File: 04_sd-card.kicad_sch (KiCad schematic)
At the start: 0 parts

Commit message: Adds SD card connector, control buttons and debug headers
Signed-off-by: Anna-Lena Marx <anna-lena.marx@web.de>
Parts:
- added C1: 22u, Capacitor_SMD:C_1206_3216Metric_Pad1.33x1.80mm_HandSolder, symbol Device:C
- added J1: Micro_SD_Card_Det2, Connector_Card:microSD_HC_Hirose_DM3AT-SF-PEJM5, symbol Connector:Micro_SD_Card_Det2
- added R1, R2, R3, R4: 22k, Resistor_SMD:R_1206_3216Metric_Pad1.30x1.75mm_HandSolder, symbol Device:R
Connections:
- new net: C1.2, J1.4 (VDD)
- new net +3.3V: C1.1, R1.1, R2.1, R3.1, R4.1
- new net GND: J1.11 (SHIELD), J1.6 (VSS)
- new net SD_CLK-SCLK: J1.5 (CLK), R2.2
- new net SD_CMD-DI: J1.3 (CMD), R3.2
- new net SD_DAT0-DO: J1.7 (DAT0), R1.2
- new net SD_DAT3-CD-CS: J1.2 (DAT3/CD), R4.2
- no-connect marks 0 -> 4

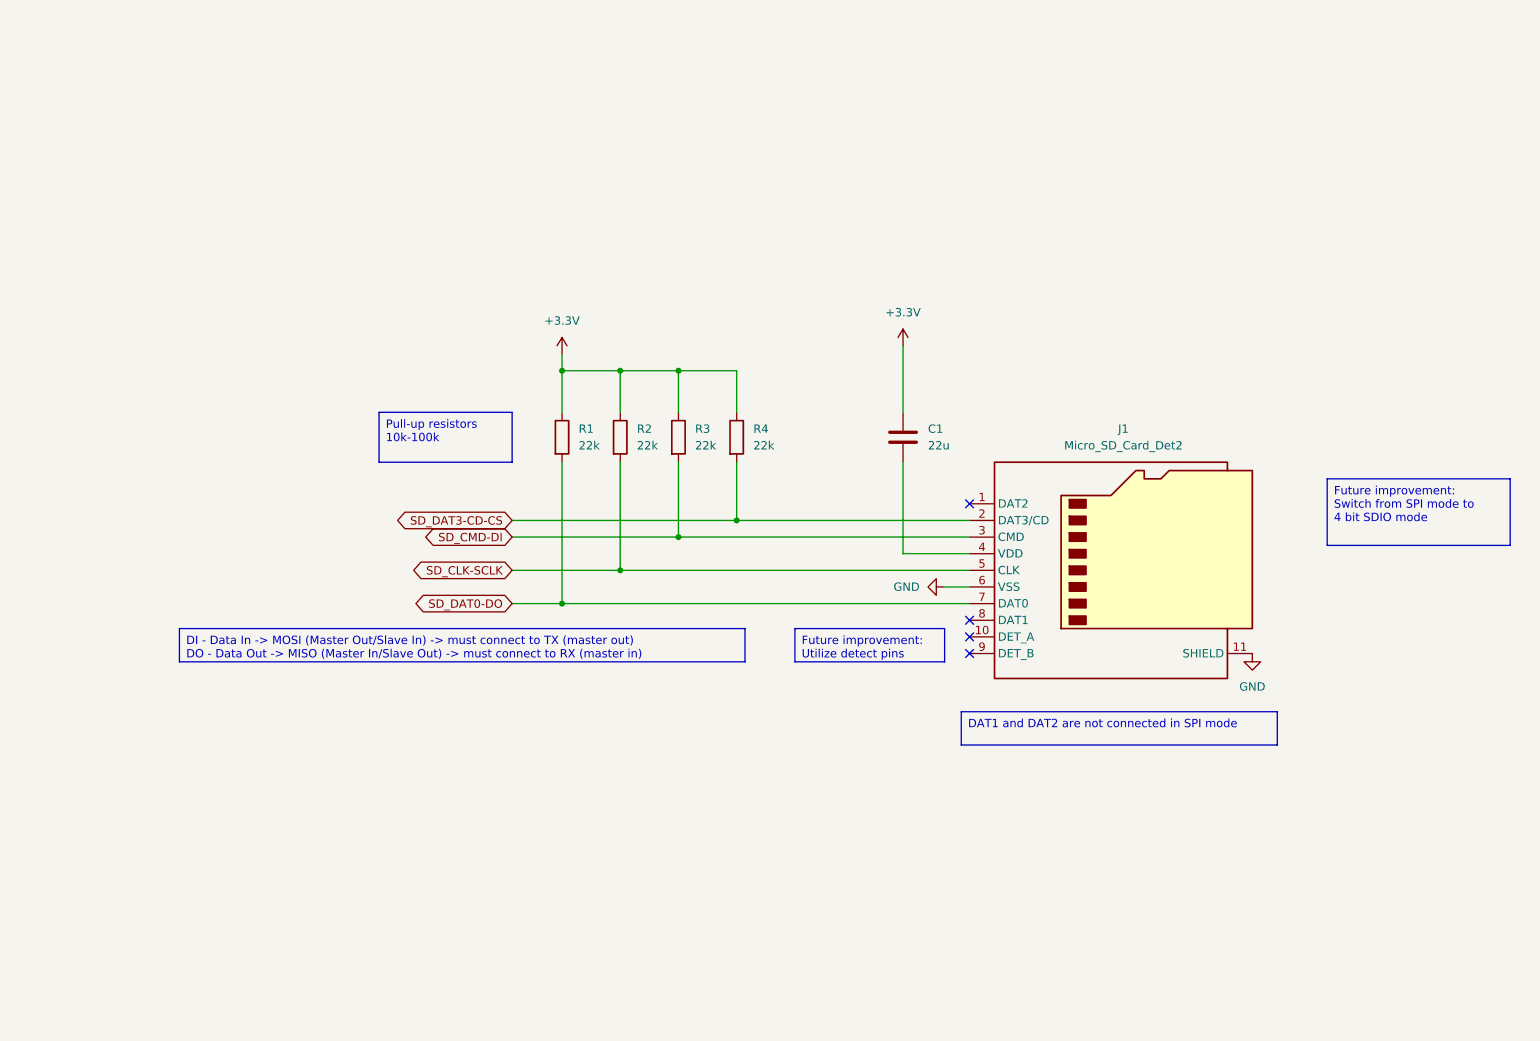
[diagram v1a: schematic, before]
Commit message: Add EPD Driver Circuit
Signed-off-by: Anna-Lena Marx <anna-lena.marx@web.de>
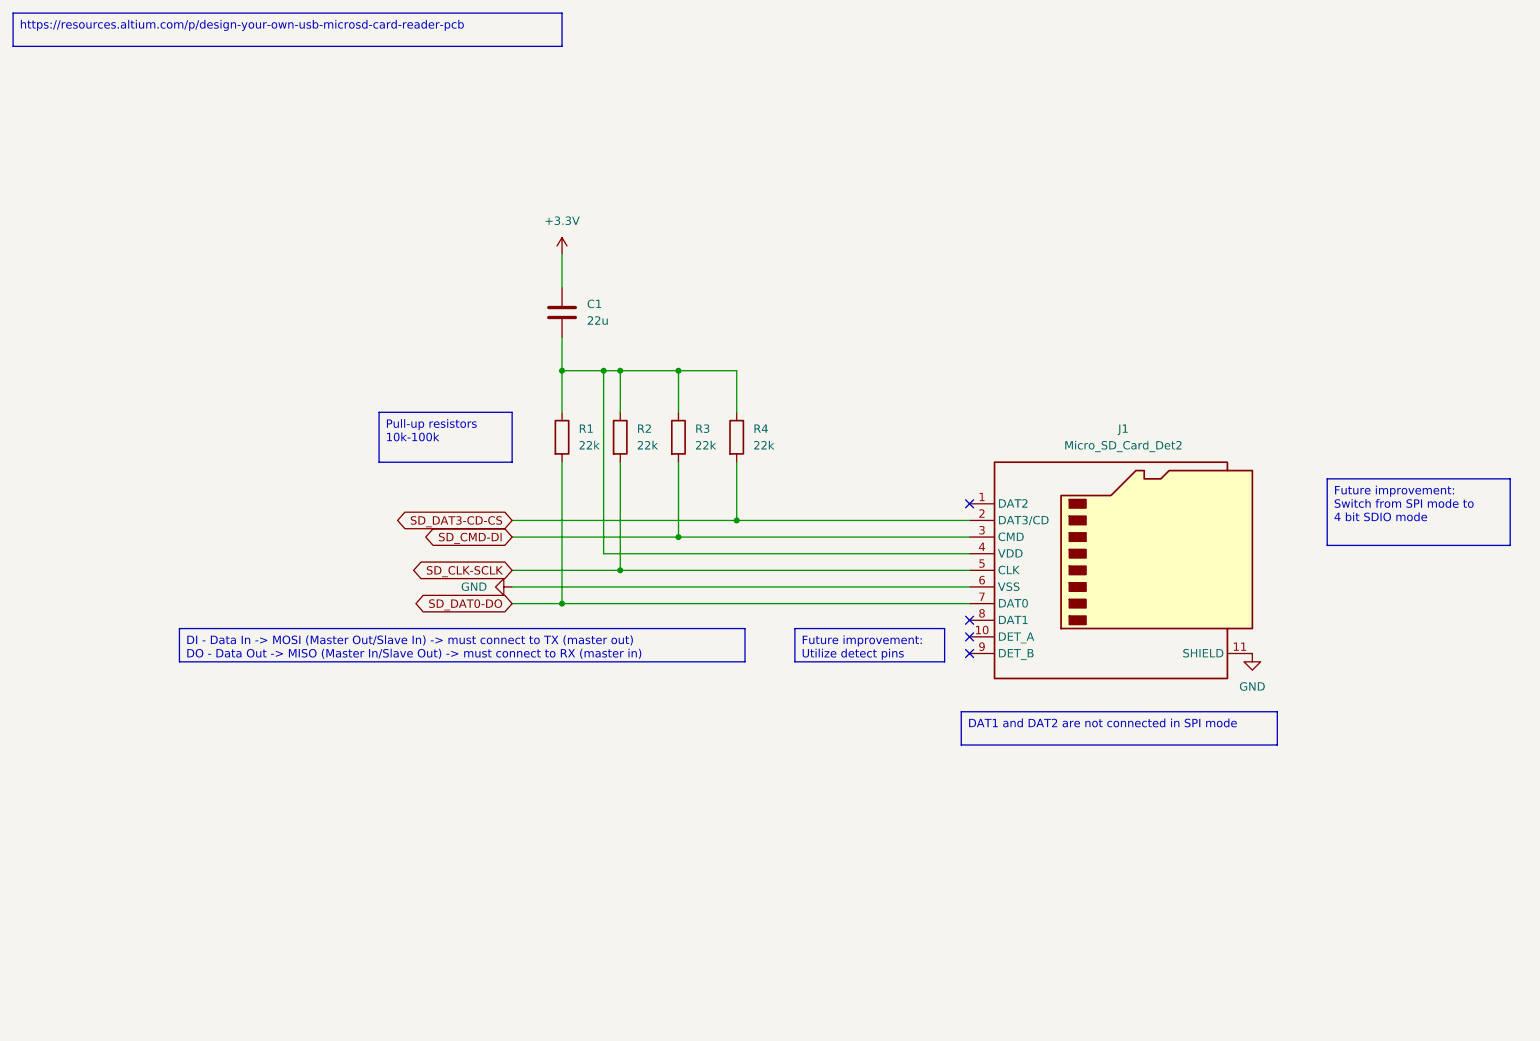
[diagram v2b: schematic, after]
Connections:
- net +3.3V: no longer R1.1, R2.1, R3.1, R4.1
- net at C1.2, J1.4 (VDD): now also R1.1, R2.1, R3.1, R4.1
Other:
- moved on the sheet: C1
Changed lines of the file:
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@@
+	)
+	(junction
+		(at 114.3 92.71)
+		(diameter 0)
+		(color 0 0 0 0)
 	)
 	(junction
@@
 	)
 	(junction
-		(at 114.3 92.71)
+		(at 105.41 67.31)
 		(diameter 0)
 		(color 0 0 0 0)
 	)
 	(junction
-		(at 105.41 67.31)
+		(at 102.87 67.31)
 		(diameter 0)
 		(color 0 0 0 0)
@@
 	(wire
 		(pts
-			(xy 114.3 67.31) (xy 105.41 67.31)
-		)
-		(stroke
-			(width 0)
-			(type default)
-		)
-	)
-	(wire
-		(pts
-			(xy 148.59 63.5) (xy 148.59 73.66)
-		)
-		(stroke
-			(width 0)
-			(type default)
-		)
-	)
-	(wire
-		(pts
 			(xy 158.75 97.79) (xy 105.41 97.79)
 		)
@@
 	(wire
 		(pts
-			(xy 148.59 95.25) (xy 158.75 95.25)
+			(xy 102.87 95.25) (xy 158.75 95.25)
 		)
 		(stroke
@@
 	(wire
 		(pts
-			(xy 154.94 100.33) (xy 158.75 100.33)
+			(xy 88.9 100.33) (xy 158.75 100.33)
+		)
+		(stroke
+			(width 0)
+			(type default)
+		)
+	)
+	(wire
+		(pts
+			(xy 96.52 67.31) (xy 102.87 67.31)
 		)
 		(stroke
@@
 	(wire
 		(pts
-			(xy 96.52 64.77) (xy 96.52 67.31)
+			(xy 114.3 67.31) (xy 123.19 67.31)
 		)
 		(stroke
@@
 	(wire
 		(pts
+			(xy 102.87 95.25) (xy 102.87 67.31)
+		)
+		(stroke
+			(width 0)
+			(type default)
+		)
+	)
+	(wire
+		(pts
 			(xy 158.75 90.17) (xy 123.19 90.17)
 		)
@@
 	(wire
 		(pts
-			(xy 148.59 81.28) (xy 148.59 95.25)
-		)
-		(stroke
-			(width 0)
-			(type default)
-		)
-	)
-	(wire
-		(pts
 			(xy 105.41 73.66) (xy 105.41 67.31)
 		)
@@
 	(wire
 		(pts
+			(xy 105.41 67.31) (xy 114.3 67.31)
+		)
+		(stroke
+			(width 0)
+			(type default)
+		)
+	)
+	(wire
+		(pts
 			(xy 123.19 90.17) (xy 123.19 81.28)
 		)
@@
 	(wire
 		(pts
-			(xy 105.41 67.31) (xy 96.52 67.31)
-		)
-		(stroke
-			(width 0)
-			(type default)
-		)
-	)
-	(wire
-		(pts
 			(xy 123.19 73.66) (xy 123.19 67.31)
 		)
@@
 	(wire
 		(pts
-			(xy 123.19 67.31) (xy 114.3 67.31)
+			(xy 102.87 67.31) (xy 105.41 67.31)
 		)
 		(stroke
@@
 	(wire
 		(pts
+			(xy 96.52 49.53) (xy 96.52 54.61)
+		)
+		(stroke
+			(width 0)
+			(type default)
+		)
+	)
+	(wire
+		(pts
 			(xy 96.52 102.87) (xy 96.52 81.28)
+		)
+		(stroke
+			(width 0)
+			(type default)
+		)
+	)
+	(wire
+		(pts
+			(xy 96.52 62.23) (xy 96.52 67.31)
 		)
 		(stroke
@@
 		(at 38.1 106.68 0)
 		(size 86.36 5.08)
+		(stroke
+			(width 0)
+			(type default)
+		)
+		(fill
+			(type none)
+		)
+		(effects
+			(font
+				(size 1.27 1.27)
+			)
+			(justify left top)
+		)
+	)
+	(text_box "https://resources.altium.com/p/design-your-own-usb-microsd-card-reader-pcb"
+		(exclude_from_sim no)
+		(at 12.7 12.7 0)
+		(size 83.82 5.08)
 		(stroke
 			(width 0)
@@
 	)
 	(symbol
-		(lib_id "power:+3.3V")
-		(at 148.59 63.5 0)
-		(unit 1)
-		(exclude_from_sim no)
-		(in_bom yes)
-		(on_board yes)
-		(dnp no)
-		(fields_autoplaced yes)
-		(property "Reference" "#PWR03"
-			(at 148.59 67.31 0)
-			(effects
-				(font
-					(size 1.27 1.27)
-				)
-				(hide yes)
-			)
-		)
-		(property "Value" "+3.3V"
-			(at 148.59 58.42 0)
-			(effects
-				(font
-					(size 1.27 1.27)
-				)
-			)
-		)
-		(property "Footprint" ""
-			(at 148.59 63.5 0)
-			(effects
-				(font
-					(size 1.27 1.27)
-				)
-				(hide yes)
-			)
-		)
-		(property "Datasheet" ""
-			(at 148.59 63.5 0)
-			(effects
-				(font
-					(size 1.27 1.27)
-				)
-				(hide yes)
-			)
-		)
-		(property "Description" "Power symbol creates a global label with name \"+3.3V\""
-			(at 148.59 63.5 0)
-			(effects
-				(font
-					(size 1.27 1.27)
-				)
-				(hide yes)
-			)
-		)
-		(pin "1"
-		)
-		(instances
-			(project ""
-				(path "/ec954637-2a8b-4662-b4a1-f88107f11cb0/5fd074b7-3c47-4717-bcdc-b0d8134ff74e"
-					(reference "#PWR03")
-					(unit 1)
-				)
-			)
-		)
-	)
-	(symbol
 		(lib_id "Device:R")
 		(at 123.19 77.47 0)
@@
 	(symbol
 		(lib_id "Device:C")
-		(at 148.59 77.47 0)
+		(at 96.52 58.42 0)
 		(unit 1)
 		(exclude_from_sim no)
@@
 		(fields_autoplaced yes)
 		(property "Reference" "C1"
-			(at 152.4 76.1999 0)
+			(at 100.33 57.1499 0)
 			(effects
 				(font
@@
 		)
 		(property "Value" "22u"
-			(at 152.4 78.7399 0)
+			(at 100.33 59.6899 0)
 			(effects
 				(font
@@
 		)
 		(property "Footprint" "Capacitor_SMD:C_1206_3216Metric_Pad1.33x1.80mm_HandSolder"
-			(at 149.5552 81.28 0)
+			(at 97.4852 62.23 0)
 			(effects
 				(font
@@
 		)
 		(property "Datasheet" "~"
-			(at 148.59 77.47 0)
+			(at 96.52 58.42 0)
 			(effects
 				(font
@@
 		)
 		(property "Description" "Unpolarized capacitor"
-			(at 148.59 77.47 0)
+			(at 96.52 58.42 0)
 			(effects
 				(font
@@
 	(symbol
 		(lib_id "power:GND")
-		(at 154.94 100.33 270)
+		(at 88.9 100.33 270)
 		(unit 1)
 		(exclude_from_sim no)
@@
 		(fields_autoplaced yes)
 		(property "Reference" "#PWR01"
-			(at 148.59 100.33 0)
+			(at 82.55 100.33 0)
 			(effects
 				(font
@@
 		)
 		(property "Value" "GND"
-			(at 151.13 100.3299 90)
+			(at 85.09 100.3299 90)
 			(effects
 				(font
@@
 		)
 		(property "Footprint" ""
-			(at 154.94 100.33 0)
+			(at 88.9 100.33 0)
 			(effects
 				(font
@@
 		)
 		(property "Datasheet" ""
-			(at 154.94 100.33 0)
+			(at 88.9 100.33 0)
 			(effects
 				(font
@@
 		)
 		(property "Description" "Power symbol creates a global label with name \"GND\" , ground"
-			(at 154.94 100.33 0)
+			(at 88.9 100.33 0)
 			(effects
 				(font
@@
 	(symbol
 		(lib_id "power:+3.3V")
-		(at 96.52 64.77 0)
+		(at 96.52 49.53 0)
 		(unit 1)
 		(exclude_from_sim no)
@@
 		(fields_autoplaced yes)
 		(property "Reference" "#PWR02"
-			(at 96.52 68.58 0)
+			(at 96.52 53.34 0)
 			(effects
 				(font
@@
 		)
 		(property "Value" "+3.3V"
-			(at 96.52 59.69 0)
+			(at 96.52 44.45 0)
 			(effects
 				(font
@@
 		)
 		(property "Footprint" ""
-			(at 96.52 64.77 0)
+			(at 96.52 49.53 0)
 			(effects
 				(font
@@
 		)
 		(property "Datasheet" ""
-			(at 96.52 64.77 0)
+			(at 96.52 49.53 0)
 			(effects
 				(font
@@
 		)
 		(property "Description" "Power symbol creates a global label with name \"+3.3V\""
-			(at 96.52 64.77 0)
-			(effects
-				(font
+			(at 96.52 49.53 0)
+			(effects
+				(font

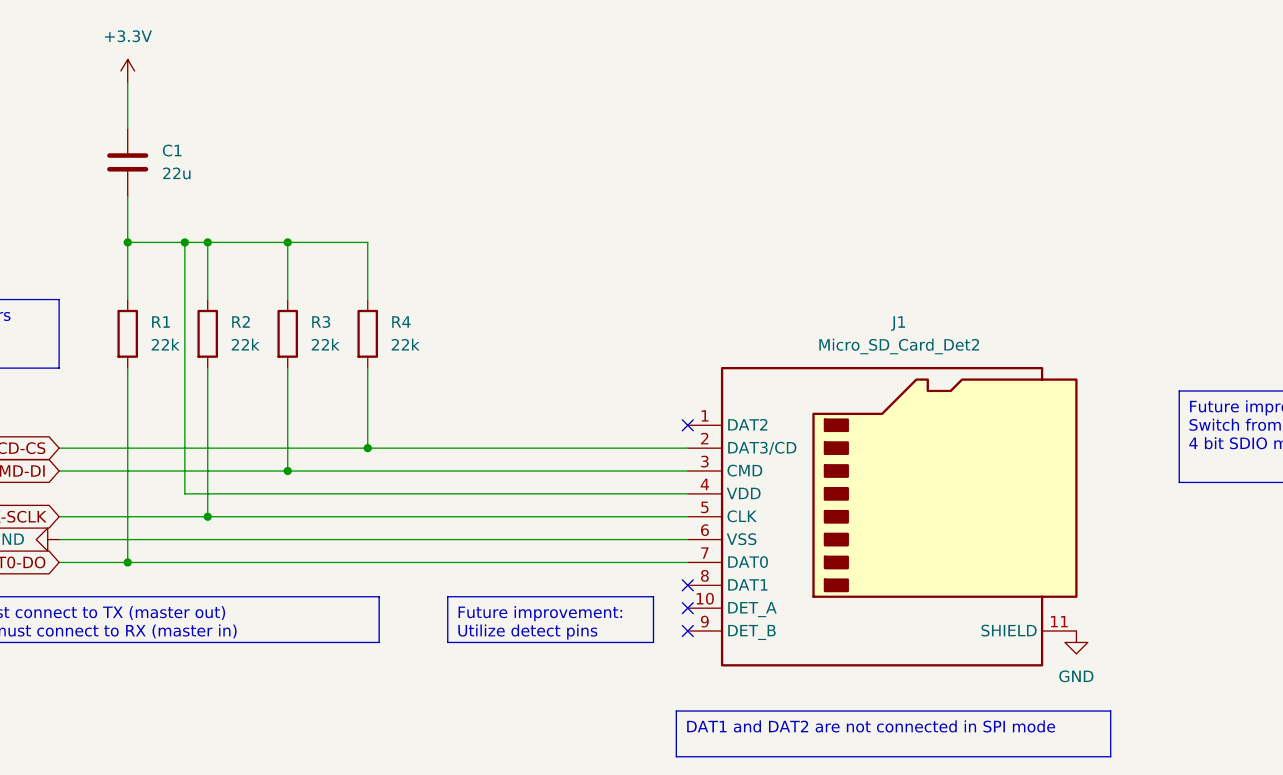
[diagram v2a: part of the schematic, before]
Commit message: Added USB-C, Battery Charging andOn/Off
Signed-off-by: Anna-Lena Marx <anna-lena.marx@web.de>
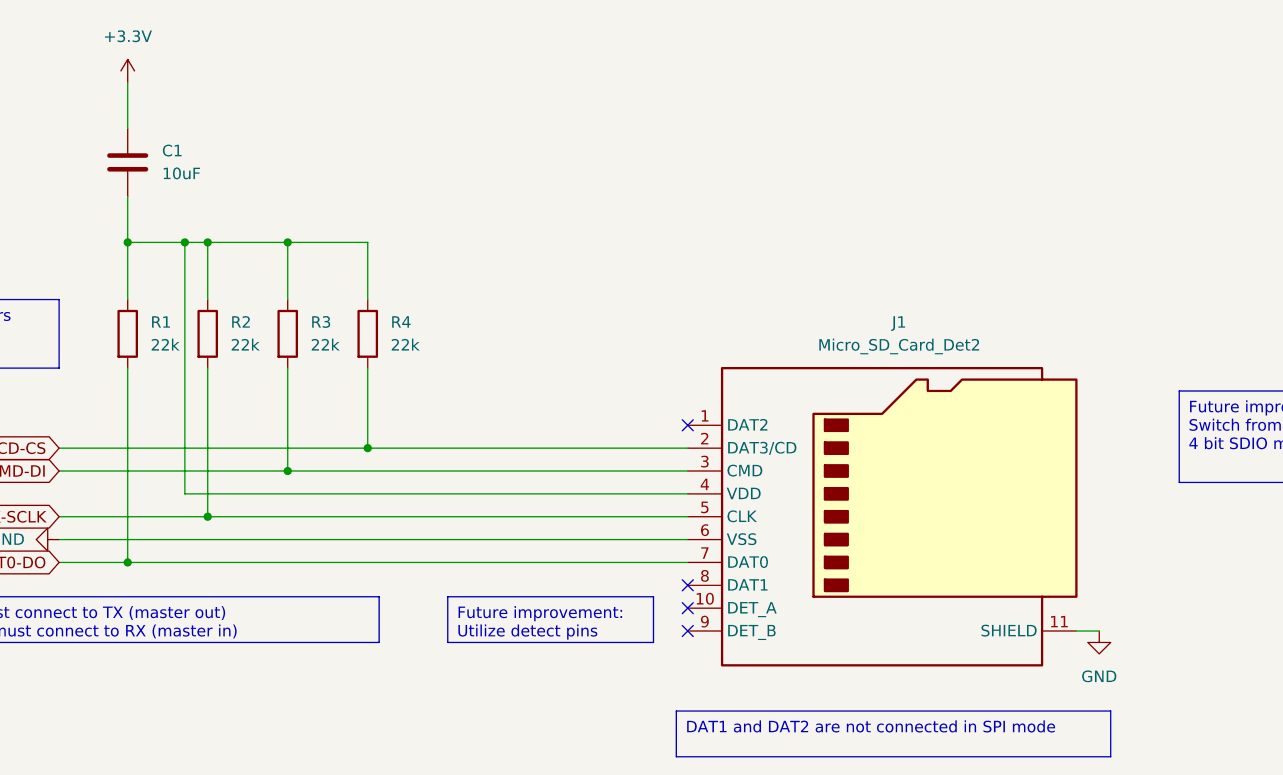
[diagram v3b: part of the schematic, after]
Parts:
- C1: value 22u -> 10uF
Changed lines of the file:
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@@
+	(wire
+		(pts
+			(xy 204.47 110.49) (xy 201.93 110.49)
+		)
+		(stroke
+			(width 0)
+			(type default)
+		)
+	)
 	(wire
 		(pts
@@
 			)
 		)
-		(property "Value" "22u"
+		(property "Value" "10uF"
 			(at 100.33 59.6899 0)
 			(effects
@@
 	(symbol
 		(lib_id "power:GND")
-		(at 201.93 110.49 0)
+		(at 204.47 110.49 0)
 		(unit 1)
 		(exclude_from_sim no)
@@
 		(fields_autoplaced yes)
 		(property "Reference" "#PWR04"
-			(at 201.93 116.84 0)
+			(at 204.47 116.84 0)
 			(effects
 				(font
@@
 		)
 		(property "Value" "GND"
-			(at 201.93 115.57 0)
+			(at 204.47 115.57 0)
 			(effects
 				(font
@@
 		)
 		(property "Footprint" ""
-			(at 201.93 110.49 0)
+			(at 204.47 110.49 0)
 			(effects
 				(font
@@
 		)
 		(property "Datasheet" ""
-			(at 201.93 110.49 0)
+			(at 204.47 110.49 0)
 			(effects
 				(font
@@
 		)
 		(property "Description" "Power symbol creates a global label with name \"GND\" , ground"
-			(at 201.93 110.49 0)
-			(effects
-				(font
+			(at 204.47 110.49 0)
+			(effects
+				(font
